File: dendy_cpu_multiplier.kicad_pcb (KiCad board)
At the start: 2 copper layers, 15.2 x 51.1 mm, 12 parts, among them J1 CLK_IN, J2 CPU Connections, U1 74ACT74, U2 ICS501

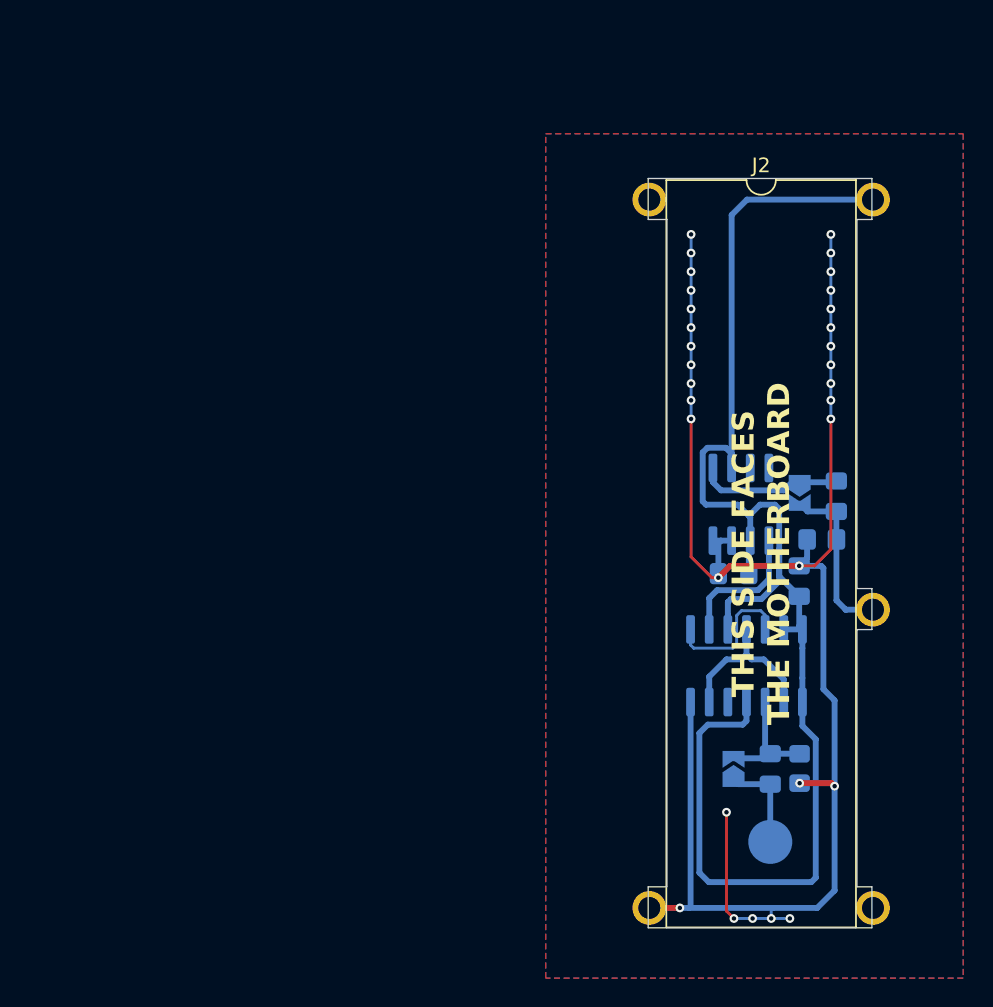
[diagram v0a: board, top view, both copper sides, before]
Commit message: Move around the components to fit into the holes of a DIP40 socket
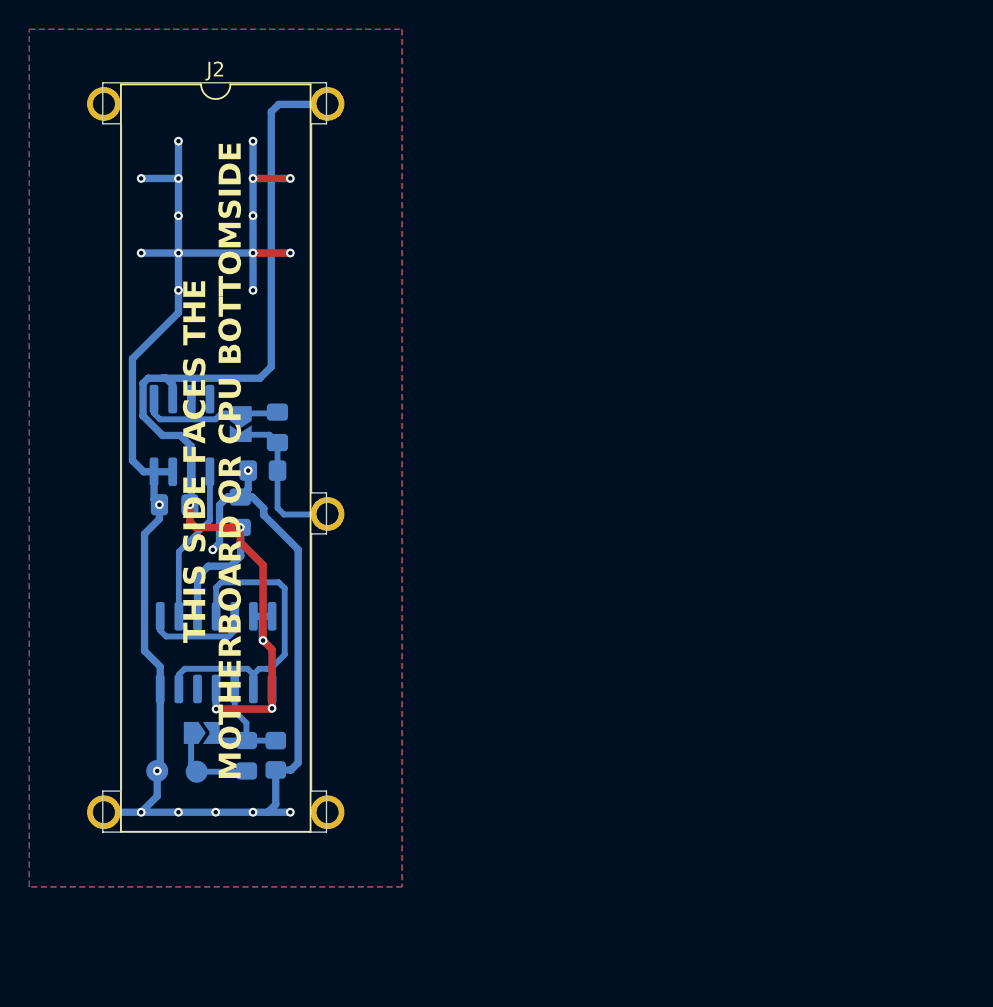
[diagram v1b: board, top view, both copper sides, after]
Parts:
- added J3: GND, TestPoint:TestPoint_Pad_D1.5mm, B.Cu at (105.2, 91.2)
- J1: footprint TestPoint:TestPoint_Pad_D3.0mm -> TestPoint:TestPoint_Pad_D1.5mm
- moved J1 39.4 mm to (107.9, 91.2)
- moved C2 38.4 mm to (110.9, 73.5)
- moved C1 38.4 mm to (106.4, 73.0)
- moved C4 38.4 mm to (113.4, 67.8)
- moved JP2 38.4 mm to (110.9, 67.5)
- moved R2 38.4 mm to (112.4, 70.7)
- moved U2 38.4 mm to (106.9, 68.3)
- moved J2 37.7 mm to (101.6, 45.7)
- moved JP1 36.3 mm to (108.3, 88.6), turned to 0 degrees
- moved U1 36.1 mm to (109.2, 83.1)
- moved C3 35.7 mm to (111.3, 90.1)
- moved R1 35.7 mm to (113.3, 90.1)
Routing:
- net VCC: track 102.4 -> 77.7 mm, vias 0 -> 5
- net Net-(U1A-D): track 11.4 -> 21.5 mm
- net GND: track 127.1 -> 120.2 mm, vias 32 -> 23
- net Net-(U1B-D): track 9.54 -> 7.36 mm
- net /CLK_DIV4: track 9.36 -> 10.7 mm
- net /DENDY_CLK: track 10.8 -> 10.0 mm
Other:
- board text added: "Rev. 1"
- board text added: "THIS SIDE FACES THE MOTHERBOARD OR CPU BOTTOMSIDE"
- board text removed: "Rev. 0"
- board text removed: "THIS SIDE FACES THE MOTHERBOARD"
